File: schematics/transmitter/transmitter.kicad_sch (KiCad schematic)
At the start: 30 parts, among them Q1 2N7000, SW1 SW_Nidec_CAS-120A1, SW2 SW_Push, U1 PIC16F18324-xSL, U2 NRF24L01_Breakout, U3 LM2937xT

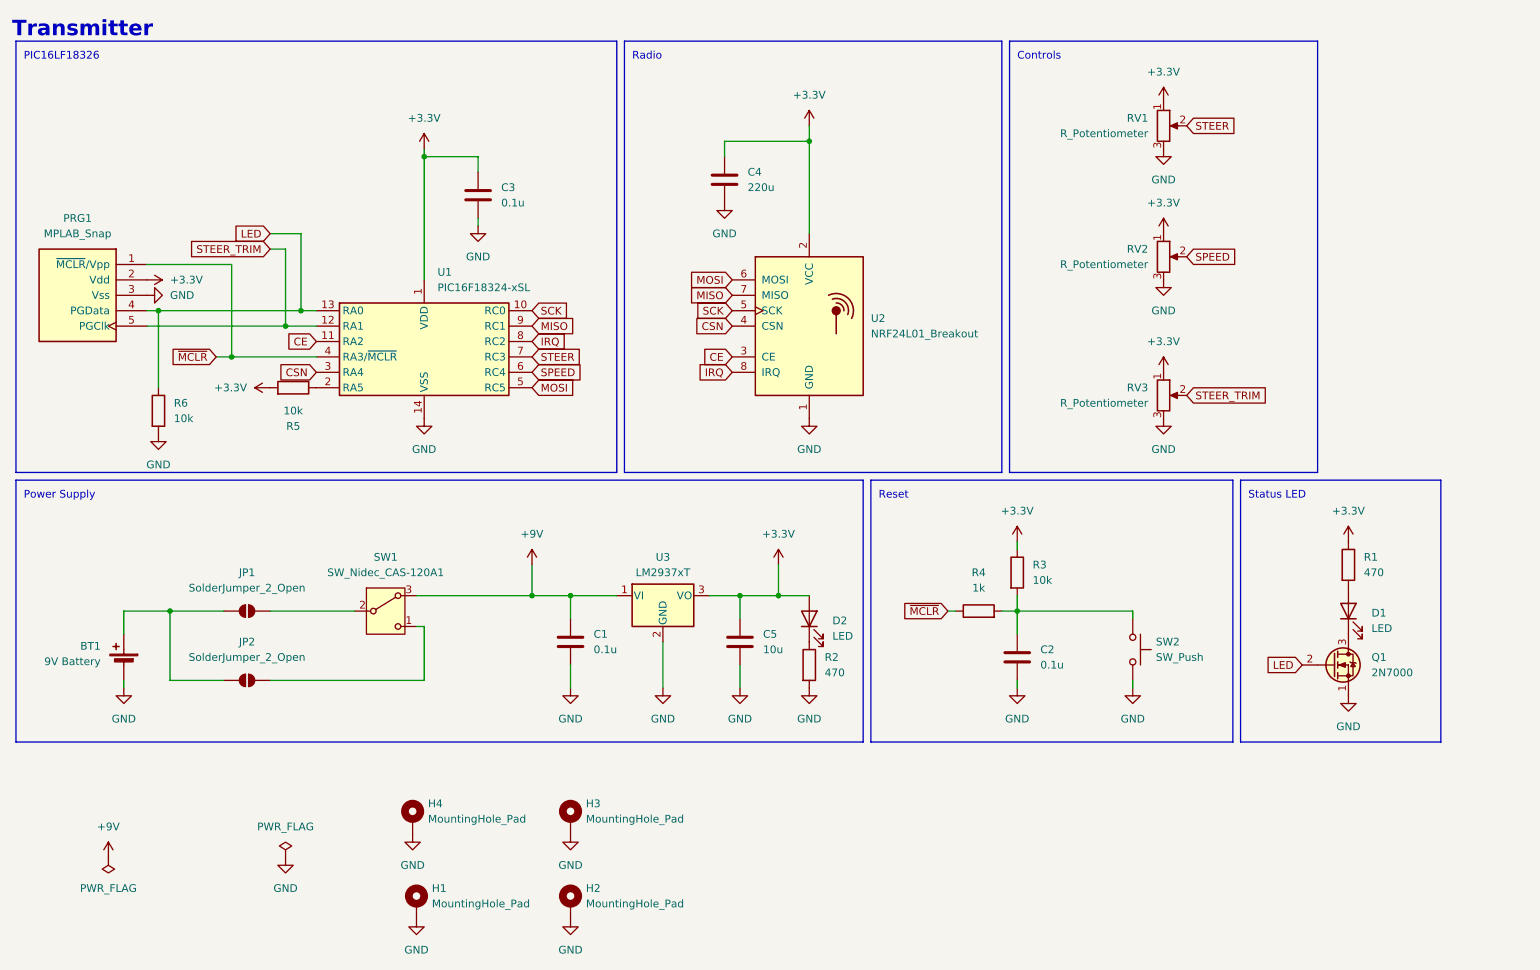
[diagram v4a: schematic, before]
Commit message: Remove trim pot, seems unnecessary
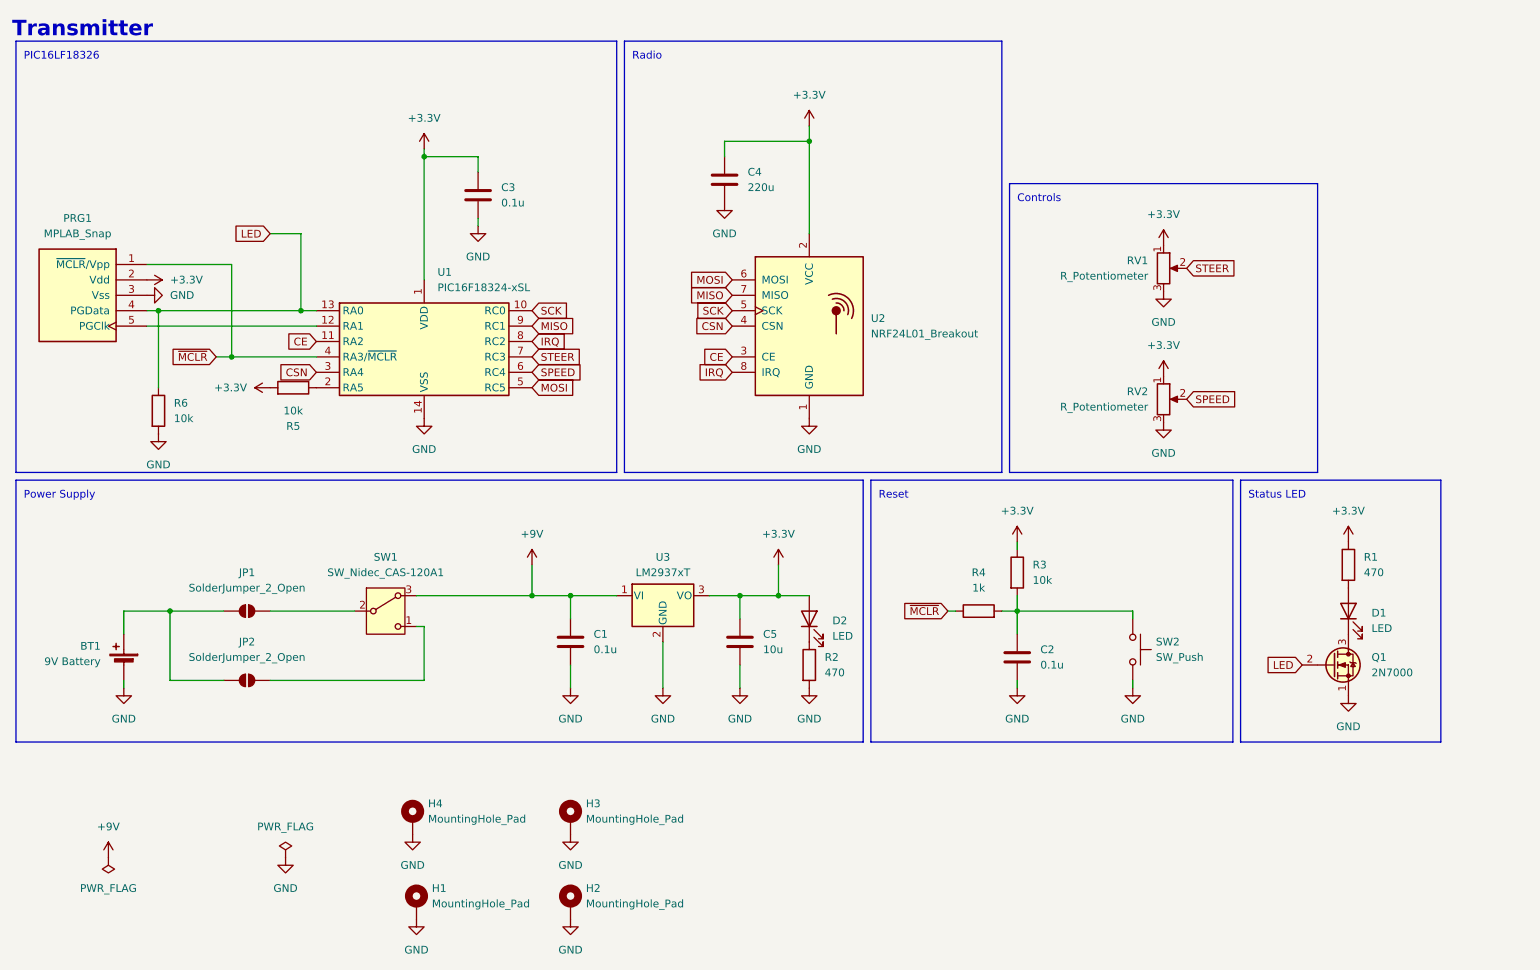
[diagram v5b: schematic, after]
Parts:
- removed RV3: R_Potentiometer, Potentiometer_THT:Potentiometer_Bourns_3386P_Vertical, symbol Device:R_Potentiometer
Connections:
- net STEER_TRIM: no longer names the net of PRG1.5 (PGClk), U1.12 (RA1)
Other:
- moved on the sheet: RV1, RV2

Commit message: Remove programing ports and reset btn from final boards
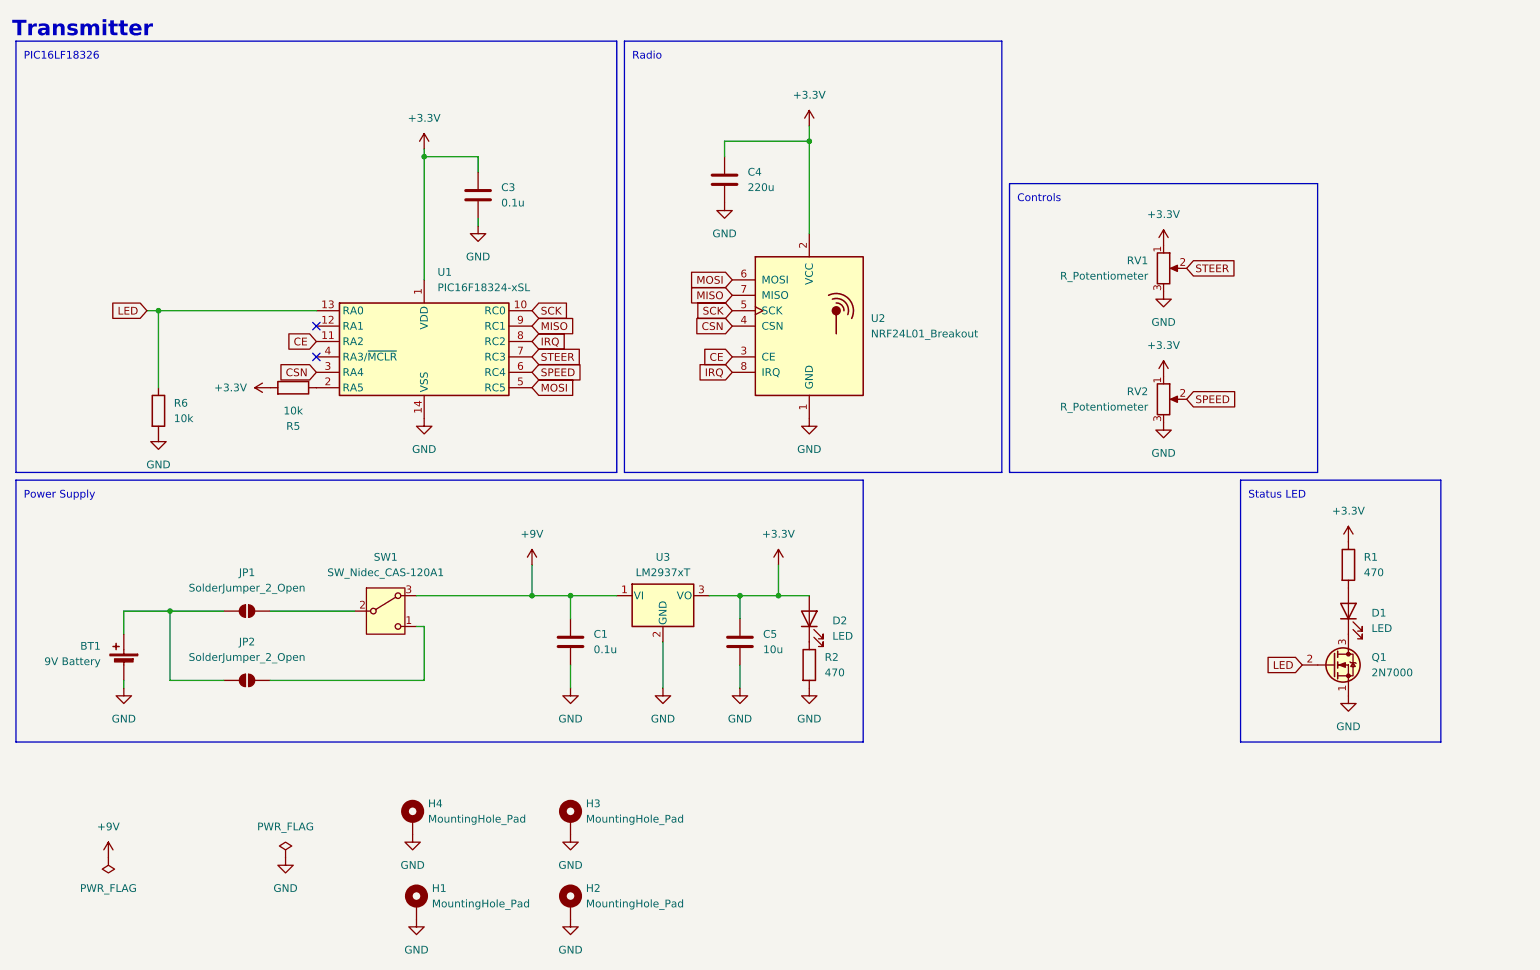
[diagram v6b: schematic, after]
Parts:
- removed C2: 0.1u, Capacitor_THT:CP_Radial_D5.0mm_P2.50mm, symbol Device:C
- removed PRG1: MPLAB_Snap, Connector_PinSocket_2.54mm:PinSocket_1x05_P2.54mm_Vertical, symbol ME218_BaseLib:MPLAB_Snap
- removed R3: 10k, Resistor_THT:R_Axial_DIN0204_L3.6mm_D1.6mm_P7.62mm_Horizontal, symbol Device:R
- removed R4: 1k, Resistor_THT:R_Axial_DIN0204_L3.6mm_D1.6mm_P7.62mm_Horizontal, symbol Device:R
- removed SW2: SW_Push, transmitter_footprints:SW_1825910-6-4, symbol Switch:SW_Push
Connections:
- net ~{MCLR}: no longer names the net of U1.4 (RA3/~{MCLR})
- no-connect marks 0 -> 2
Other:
- note removed: "Reset"

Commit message: Updated switch with better 3d model
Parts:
- removed H3: MountingHole_Pad, MountingHole:MountingHole_2.5mm_Pad_TopBottom, symbol Mechanical:MountingHole_Pad
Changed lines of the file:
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@@
-	)
-	(symbol
-		(lib_id "Mechanical:MountingHole_Pad")
-		(at 118.11 166.37 0)
-		(unit 1)
-		(exclude_from_sim yes)
-		(in_bom no)
-		(on_board yes)
-		(dnp no)
-		(fields_autoplaced yes)
-		(property "Reference" "H3"
-			(at 120.65 163.8299 0)
-			(effects
-				(font
-					(size 1.27 1.27)
-				)
-				(justify left)
-			)
-		)
-		(property "Value" "MountingHole_Pad"
-			(at 120.65 166.3699 0)
-			(effects
-				(font
-					(size 1.27 1.27)
-				)
-				(justify left)
-			)
-		)
-		(property "Footprint" "MountingHole:MountingHole_2.5mm_Pad_TopBottom"
-			(at 118.11 166.37 0)
-			(effects
-				(font
-					(size 1.27 1.27)
-				)
-				(hide yes)
-			)
-		)
-		(property "Datasheet" "~"
-			(at 118.11 166.37 0)
-			(effects
-				(font
-					(size 1.27 1.27)
-				)
-				(hide yes)
-			)
-		)
-		(property "Description" "Mounting Hole with connection"
-			(at 118.11 166.37 0)
-			(effects
-				(font
-					(size 1.27 1.27)
-				)
-				(hide yes)
-			)
-		)
-		(property "Mfn" ""
-			(at 118.11 166.37 0)
-			(effects
-				(font
-					(size 1.27 1.27)
-				)
-				(hide yes)
-			)
-		)
-		(property "Mfn PN" ""
-			(at 118.11 166.37 0)
-			(effects
-				(font
-					(size 1.27 1.27)
-				)
-				(hide yes)
-			)
-		)
-		(property "Supplier" ""
-			(at 118.11 166.37 0)
-			(effects
-				(font
-					(size 1.27 1.27)
-				)
-				(hide yes)
-			)
-		)
-		(property "Supplier PN" ""
-			(at 118.11 166.37 0)
-			(effects
-				(font
-					(size 1.27 1.27)
-				)
-				(hide yes)
-			)
-		)
-		(pin "1"
-		)
-		(instances
-			(project "transmitter"
-				(path "/8cd5d3cf-8985-42c2-bd7d-5d07b5ac3cd8"
-					(reference "H3")
-					(unit 1)
-				)
-			)
-		)
 	)
 	(symbol
@@
 					(unit 1)
 				)
-			)
-		)
-	)
-	(symbol
-		(lib_id "power:GND")
-		(at 118.11 168.91 0)
-		(unit 1)
-		(exclude_from_sim no)
-		(in_bom yes)
-		(on_board yes)
-		(dnp no)
-		(fields_autoplaced yes)
-		(property "Reference" "#PWR032"
-			(at 118.11 175.26 0)
-			(effects
-				(font
-					(size 1.27 1.27)
-				)
-				(hide yes)
-			)
-		)
-		(property "Value" "GND"
-			(at 118.11 173.99 0)
-			(effects
-				(font
-					(size 1.27 1.27)
-				)
-			)
-		)
-		(property "Footprint" ""
-			(at 118.11 168.91 0)
-			(effects
-				(font
-					(size 1.27 1.27)
-				)
-				(hide yes)
-			)
-		)
-		(property "Datasheet" ""
-			(at 118.11 168.91 0)
-			(effects
-				(font
-					(size 1.27 1.27)
-				)
-				(hide yes)
-			)
-		)
-		(property "Description" "Power symbol creates a global label with name \"GND\" , ground"
-			(at 118.11 168.91 0)
-			(effects
-				(font
-					(size 1.27 1.27)
-				)
-				(hide yes)
-			)
-		)
-		(pin "1"
-		)
-		(instances
-			(project "transmitter"
-				(path "/8cd5d3cf-8985-42c2-bd7d-5d07b5ac3cd8"
-					(reference "#PWR032")
-					(unit 1)
-				)

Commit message: Add trim pot to transmitter
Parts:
- added RV3: R_Potentiometer, Potentiometer_THT:Potentiometer_Bourns_3386P_Vertical, symbol Device:R_Potentiometer
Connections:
- net +3.3V: now also RV3.1
- net GND: now also RV3.3, RV3.S1, RV3.S2
- net TRIM: now reaches U1.12 (RA1)
- net TRIM: now also RV3.2
- no-connect marks 2 -> 1
